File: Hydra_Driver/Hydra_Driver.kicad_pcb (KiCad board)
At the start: 2 copper layers, 69 x 42 mm, 104 parts, among them IC1 ESP32-S3-WROOM-1-N4, IC2 DRV8313RHHR, IC3 DRV8313RHHR, J1 USB4105-GF-A, J10 Conn_01x03, J11 Conn_01x04, J12 Conn_01x03, J13 Conn_01x02, J2 Conn_01x02, J3 Conn_01x06, J4 Conn_01x03, J5 Conn_01x04, J6 Conn_01x03, J7 Conn_01x02, J8 Conn_01x03, J9 Conn_01x06, SW1 SW_SPST, SW2 SW_SPST, U1 USBLC6-2SC6, U2 MIC5365-3.3YC5, U3 74HC32, U4 INA199xxDCK, U5 INA199xxDCK, U6 74HC32, U7 INA199xxDCK, U8 INA199xxDCK

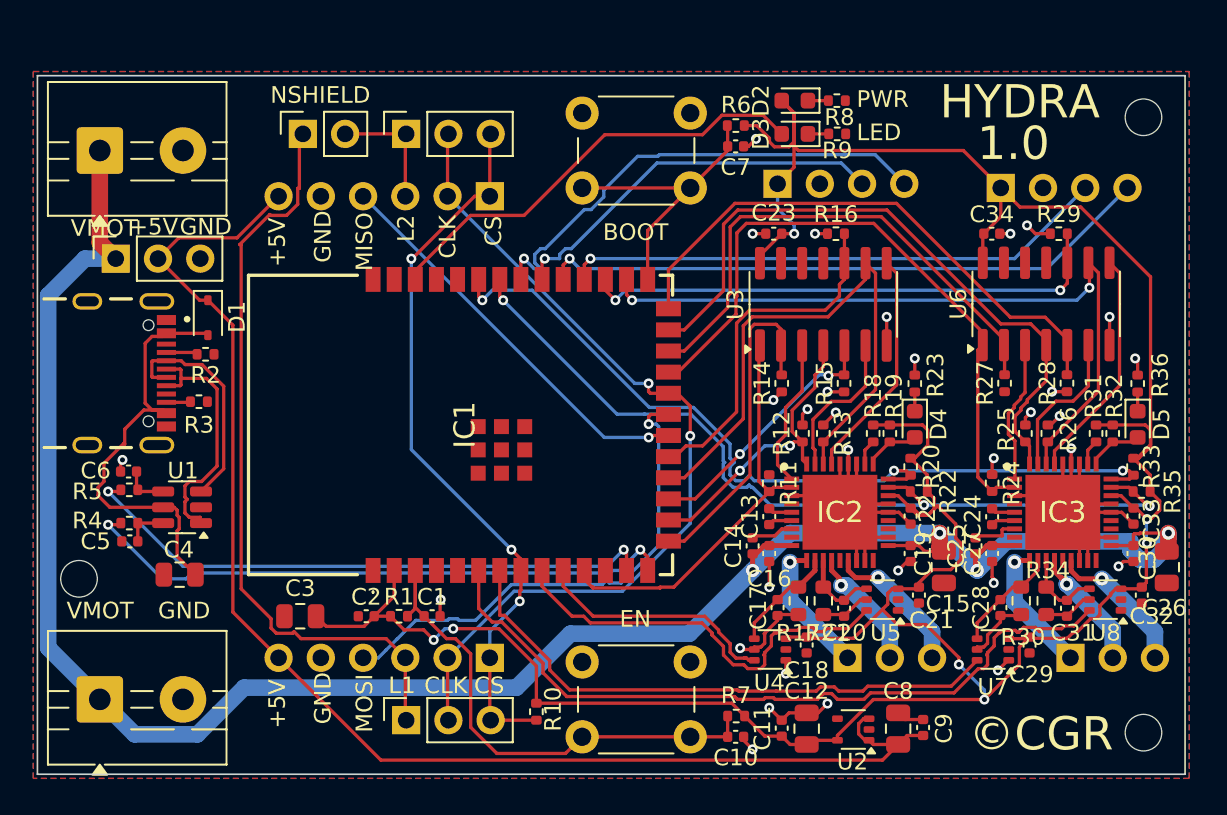
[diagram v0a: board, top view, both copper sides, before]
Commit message: Mostly finished applying changes from design review
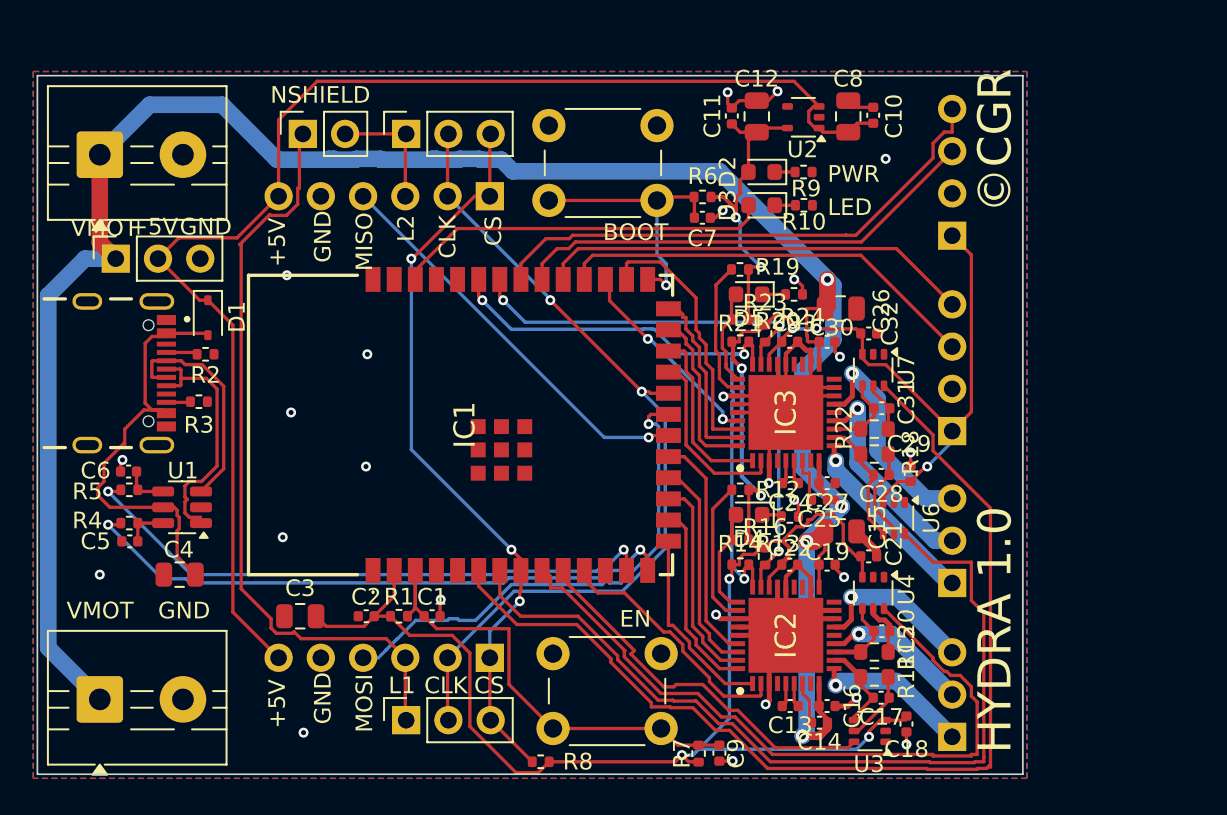
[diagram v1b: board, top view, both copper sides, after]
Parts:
- removed C23, C34: 0.1u, Capacitor_SMD:C_0402_1005Metric
- removed the R11 at (44.0, 24.5)
- removed the R12 at (46.0, 21.5)
- removed the R13 at (47.2, 21.5)
- removed the R14 at (44.8, 18.5)
- removed the R15 at (48.5, 18.5)
- removed the R16 at (48.0, 9.50)
- removed the R24 at (57.4, 24.5)
- removed R25, R26, R27, R28, R29: 3.3k, Resistor_SMD:R_0402_1005Metric
- removed REF** (x3): MountingHole_2.2mm_M2, MountingHole:MountingHole_2.2mm_M2
- removed the U3 at (47.2, 13.8)
- removed the U6 at (60.6, 13.7)
- J11, J5: footprint Connector_PinHeader_2.54mm:PinHeader_1x04_P2.54mm_Vertical -> Connector_PinHeader_2.54mm:PinHeader_1x04_P2.54mm_Horizontal
- J12, J6: footprint Connector_PinHeader_2.54mm:PinHeader_1x03_P2.54mm_Vertical -> Connector_PinHeader_2.54mm:PinHeader_1x03_P2.54mm_Horizontal
- moved U2 36.9 mm to (46.0, 2.50)
- moved C10 36.9 mm to (50.2, 2.38)
- moved C11 36.9 mm to (41.8, 2.42)
- moved C12 36.9 mm to (43.2, 2.45)
- moved C8 36.9 mm to (48.8, 2.45)
- moved C26 25.0 mm to (48.3, 14.0), turned to 180 degrees
- moved R21 24.8 mm to (42.3, 16.0), turned to 180 degrees
- moved D5 24.6 mm to (42.8, 13.2), turned to 180 degrees
- moved R23 24.5 mm to (43.8, 15.5), turned to 90 degrees
- moved R19 23.6 mm to (42.2, 11.7), turned to 0 degrees
- moved R20 23.4 mm to (42.2, 14.7), turned to 0 degrees
- moved C33 23.2 mm to (45.2, 16.0), turned to 180 degrees
- moved C32 22.7 mm to (50.0, 15.5), turned to 180 degrees
- moved C30 22.4 mm to (47.5, 16.0), turned to 180 degrees
- moved R24 21.3 mm to (45.5, 13.2), turned to 0 degrees
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- renumbered C9 to C10, C10 to C9, R9 to R10, R17 to R11, R18 to R12, R19 to R13, R20 to R14, R21 to R15, R22 to R16, R23 to R17, R30 to R18, R31 to R19, R32 to R20, R33 to R21, R34 to R22, R35 to R23, R36 to R24, R10 to R8, R8 to R9, U4 to U3, U5 to U4, U7 to U6, U8 to U7
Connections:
- net /IN1HA renamed /IN1A
- net /IN1HB renamed /IN1B
- net /IN2HA renamed /IN2A
- net /IN2HB renamed /IN2B
- net /IN3HA renamed /IN3A
- net /IN3HB renamed /IN3B
- IC1 pad 15: /IN1LA -> /EN1A
- IC1 pad 17: /IN2LA -> /EN2A
- IC1 pad 19: /IN3LA -> /EN3A
- IC1 pad 24: /IN1LB -> /EN1B
- IC1 pad 26: /IN2LB -> /EN2B
- IC1 pad 29: /IN3LB -> /EN3B
- IC1 pad 30: /SDA2 -> /SDA1
- IC1 pad 31: /SCL2 -> /SCL1
- IC1 pad 32: /SDA1 -> /SDA2
- IC1 pad 33: /SCL1 -> /SCL2
- IC2 pad 1: /Driver_Unit/EN1 -> /EN1A
- IC2 pad 33: /Driver_Unit/EN3 -> /EN3A
- IC2 pad 35: /Driver_Unit/EN2 -> /EN2A
- IC3 pad 1: /Driver_Unit1/EN1 -> /EN1B
- IC3 pad 33: /Driver_Unit1/EN3 -> /EN3B
- IC3 pad 35: /Driver_Unit1/EN2 -> /EN2B
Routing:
- net /IN2LB: track 33.5 -> 0.00 mm
- net /IN3LB: track 32.1 -> 0.00 mm, vias 2 -> 0
- net /IN1LB: track 31.5 -> 0.00 mm
- net +3.3V: track 185.1 -> 155.3 mm, vias 7 -> 10
- net /IN2B: track 39.9 -> 10.2 mm
- net /IN1B: track 39.7 -> 11.1 mm
- net /IN3B: track 44.4 -> 15.9 mm, vias 2 -> 0
- net /IN3A: track 34.7 -> 13.1 mm
- net /IN3LA: track 21.3 -> 0.00 mm
- net /IN1LA: track 20.2 -> 0.00 mm
- net /SENSE2A: track 25.4 -> 43.1 mm
- net /SENSE1B: track 34.6 -> 51.9 mm
- net /SENSE2B: track 45.4 -> 62.2 mm
- net /IN2LA: track 15.5 -> 0.00 mm, vias 2 -> 0
- net /RESET: track 52.0 -> 37.6 mm
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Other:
- board size 69 x 42 mm -> 59.2 x 42 mm
- board text added: "HYDRA 1.0"
- board text removed: "+3.3"
- board text removed: "SCL1"
- board text removed: "SCL2"
- board text removed: "SDA1"
- board text removed: "SDA2"

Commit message: Finished Hydra modifications
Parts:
- added REF**: MountingHole_2.2mm_M2, MountingHole:MountingHole_2.2mm_M2, F.Cu at (39.4, 39.4)
- added REF**: MountingHole_2.2mm_M2, MountingHole:MountingHole_2.2mm_M2, F.Cu at (50.2, 10.0)
- added REF**: MountingHole_2.2mm_M2, MountingHole:MountingHole_2.2mm_M2, F.Cu at (2.60, 30.0)
- U2: value MIC5365-3.3YC5 -> MIC5504-3.3YM5-TR; footprint Package_TO_SOT_SMD:SOT-353_SC-70-5 -> Touchstone:SOT-23-5_MC_MCH
- moved C10 6.94 mm to (37.6, 34.7)
- moved SW2 5.06 mm to (30.7, 39.8), turned to 90 degrees
- moved R8 3.55 mm to (26.7, 41.2), turned to 180 degrees
- moved R7 2.65 mm to (42.4, 40.7)
- moved C8 1.25 mm to (50.0, 2.45)
- moved C9 1.25 mm to (51.5, 2.38)
- moved U2 0.58 mm to (46.6, 2.70)
- renumbered C9 to C10, C24 to C23, C25 to C24, C26 to C25, C27 to C26, C28 to C27, C29 to C28, C30 to C29, C31 to C30, C32 to C31, C33 to C32, C10 to C9, U6 to U5, U7 to U6
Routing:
- net GND: track 99.1 -> 125.9 mm, vias 25 -> 42
- net /CHIP_PU: track 28.8 -> 38.1 mm
- net +5V: track 80.5 -> 83.6 mm
- net +3.3V: track 155.3 -> 158.4 mm
- net /CS: track 44.9 -> 43.8 mm
- net /SENSE2A: track 43.1 -> 44.1 mm
- net /SENSE1A: track 22.9 -> 23.8 mm
- net /OUT1B: track 11.3 -> 12.1 mm
- net /OUT1A: track 9.53 -> 10.3 mm
- net /SENSE1B: track 51.9 -> 52.6 mm
- net VMOT: track 137.1 -> 136.6 mm
- net /SCL2: track 32.1 -> 31.5 mm
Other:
- board text added: "+3.3"
- board text added: "FAULT"
- board text added: "I2C1"
- board text added: "I2C2"
- board text added: "SCL"
- board text added: "SDA"
- board text removed: "HYDRA 1.0"

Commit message: Finished updating shield board with changes
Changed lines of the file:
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@@
-	)
-	(segment
-		(start 3.75 4.75)
-		(end 3.75 10.04)
-		(width 1)
-		(layer "F.Cu")
-		(net 3)
-	)
-	(segment
-		(start 3.75 10.04)
-		(end 4.71 11)
-		(width 1)
-		(layer "F.Cu")
-		(net 3)
 	)
 	(segment
@@
 	)
 	(segment
+		(start 4.71 5.71)
+		(end 3.75 4.75)
+		(width 1)
+		(layer "B.Cu")
+		(net 3)
+	)
+	(segment
 		(start 14.409 5)
 		(end 14.409 5.051)
@@
 		(width 1)
 		(layer "B.Cu")
+		(net 3)
+	)
+	(segment
+		(start 4.71 11)
+		(end 4.71 5.71)
+		(width 1)
+		(layer "B.Cu")
